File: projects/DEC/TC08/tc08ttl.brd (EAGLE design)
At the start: 393.8 x 298.4 mm, 144 parts, among them IC1 74LS30N, IC2 74LS00N, IC3 74LS04N, IC4 74LS74N, IC5 74LS74N, IC6 74LS30N, IC7 74LS00N, IC8 74LS00N, IC9 74LS04N

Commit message: Removed power polygons for signal "NC" from nearly all drawings.  It is cleaner to just approve the unconnected input pins.  The exception is the W707, which has unconnected power pins.  Those would otherwise be connected implicitly, so an explicit "NC" is needed.
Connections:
- removed net NC: A04.T2, A04.V2, A05.E2, A05.H2, A05.T2, A05.V2, A18.H2, A18.L2, A18.M2, A20.H2, A20.L2, A20.M2, A21.H2, A21.L2, A21.M2, A24.A2, A24.B2, A24.J2, A26.D1, AB01.BN1, AB01.BP1, B05.L2, B18.H2, B18.L2, B18.M2, B20.H2, B20.L2, B20.M2, B22.R2, C02.P2, C02.S2, C03.P2, C03.S2, C03.U2, C07.N1, C07.P1, C07.R1, C07.S2, C07.T2, C07.U2, D04.T2, D04.V2, D05.E2, D05.H2, D05.T2, D05.V2, D14.B1, D14.D1, D14.E1, D14.F1, D14.J1, D14.N2, D14.P2, D14.R2, D14.S2, D14.U2, D15.M2, D15.P2, D15.R2, D15.T2
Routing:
- removed copper zone on layer 8, net NC
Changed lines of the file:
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@@
 <layer number="6" name="Route6" color="1" fill="8" visible="no" active="no"/>
 <layer number="7" name="Route7" color="4" fill="8" visible="no" active="no"/>
-<layer number="8" name="NC$" color="1" fill="2" visible="yes" active="yes"/>
 <layer number="9" name="Route9" color="4" fill="2" visible="no" active="no"/>
 <layer number="10" name="Route10" color="1" fill="7" visible="no" active="no"/>
@@
 <contactref element="C14" pad="A1"/>
 <contactref element="C14" pad="D1"/>
-<contactref element="C14" pad="K1"/>
 <contactref element="C14" pad="F2"/>
-<wire x1="207.9625" y1="142.875" x2="204.7875" y2="133.35" width="0" layer="19" extent="1-1"/>
-<wire x1="204.7875" y1="133.35" x2="198.4375" y2="127" width="0" layer="19" extent="1-1"/>
-<wire x1="198.4375" y1="127" x2="201.6125" y2="117.475" width="0" layer="19" extent="1-1"/>
+<contactref element="C14" pad="K1"/>
+<wire x1="204.7875" y1="133.35" x2="207.9625" y2="142.875" width="0" layer="19" extent="1-1"/>
+<wire x1="198.4375" y1="127" x2="204.7875" y2="133.35" width="0" layer="19" extent="1-1"/>
+<wire x1="201.6125" y1="117.475" x2="198.4375" y2="127" width="0" layer="19" extent="1-1"/>
 <wire x1="207.9625" y1="117.475" x2="201.6125" y2="117.475" width="0" layer="19" extent="1-1"/>
-<wire x1="198.4375" y1="127" x2="176.2125" y2="123.825" width="0" layer="19" extent="1-1"/>
-<wire x1="201.6125" y1="117.475" x2="195.2625" y2="92.075" width="0" layer="19" extent="1-1"/>
+<wire x1="176.2125" y1="123.825" x2="198.4375" y2="127" width="0" layer="19" extent="1-1"/>
+<wire x1="195.2625" y1="92.075" x2="201.6125" y2="117.475" width="0" layer="19" extent="1-1"/>
 </signal>
 <signal name="N$17">
@@
 <contactref element="A21" pad="V2"/>
 </signal>
-<signal name="NC">
-<contactref element="AB01" pad="BN1"/>
-<contactref element="AB01" pad="BP1"/>
-<contactref element="A04" pad="T2"/>
-<contactref element="A04" pad="V2"/>
-<contactref element="A05" pad="T2"/>
-<contactref element="A05" pad="V2"/>
-<contactref element="A24" pad="A2"/>
-<contactref element="A24" pad="B2"/>
-<contactref element="A26" pad="D1"/>
-<contactref element="A05" pad="E2"/>
-<contactref element="A05" pad="H2"/>
-<contactref element="D05" pad="T2"/>
-<contactref element="D05" pad="V2"/>
-<contactref element="D04" pad="V2"/>
-<contactref element="D04" pad="T2"/>
-<contactref element="D05" pad="E2"/>
-<contactref element="D05" pad="H2"/>
-<contactref element="A24" pad="J2"/>
-<contactref element="C07" pad="U2"/>
-<contactref element="C07" pad="S2"/>
-<contactref element="C07" pad="T2"/>
-<contactref element="C07" pad="P1"/>
-<contactref element="C07" pad="N1"/>
-<contactref element="C07" pad="R1"/>
-<contactref element="B22" pad="R2"/>
-<contactref element="D15" pad="M2"/>
-<contactref element="D15" pad="R2"/>
-<contactref element="D15" pad="T2"/>
-<contactref element="D15" pad="P2"/>
-<contactref element="D14" pad="U2"/>
-<contactref element="D14" pad="S2"/>
-<contactref element="D14" pad="R2"/>
-<contactref element="D14" pad="P2"/>
-<contactref element="D14" pad="N2"/>
-<contactref element="A21" pad="M2"/>
-<contactref element="A21" pad="L2"/>
-<contactref element="A21" pad="H2"/>
-<contactref element="B20" pad="H2"/>
-<contactref element="B20" pad="M2"/>
-<contactref element="B20" pad="L2"/>
-<contactref element="A20" pad="L2"/>
-<contactref element="A20" pad="M2"/>
-<contactref element="A20" pad="H2"/>
-<contactref element="B18" pad="H2"/>
-<contactref element="B18" pad="M2"/>
-<contactref element="B18" pad="L2"/>
-<contactref element="A18" pad="L2"/>
-<contactref element="A18" pad="H2"/>
-<contactref element="A18" pad="M2"/>
-<contactref element="B05" pad="L2"/>
-<contactref element="C02" pad="S2"/>
-<contactref element="C02" pad="P2"/>
-<contactref element="C03" pad="P2"/>
-<contactref element="C03" pad="S2"/>
-<contactref element="C03" pad="U2"/>
-<contactref element="D14" pad="D1"/>
-<contactref element="D14" pad="B1"/>
-<contactref element="D14" pad="E1"/>
-<contactref element="D14" pad="F1"/>
-<contactref element="D14" pad="J1"/>
-<polygon width="0.254" layer="8" orphans="yes">
-<vertex x="-0.0358" y="0.0126"/>
-<vertex x="414.02" y="0.0126"/>
-<vertex x="414.02" y="298.4501"/>
-<vertex x="-0.0358" y="298.4501"/>
-</polygon>
-</signal>
 <signal name="+11V">

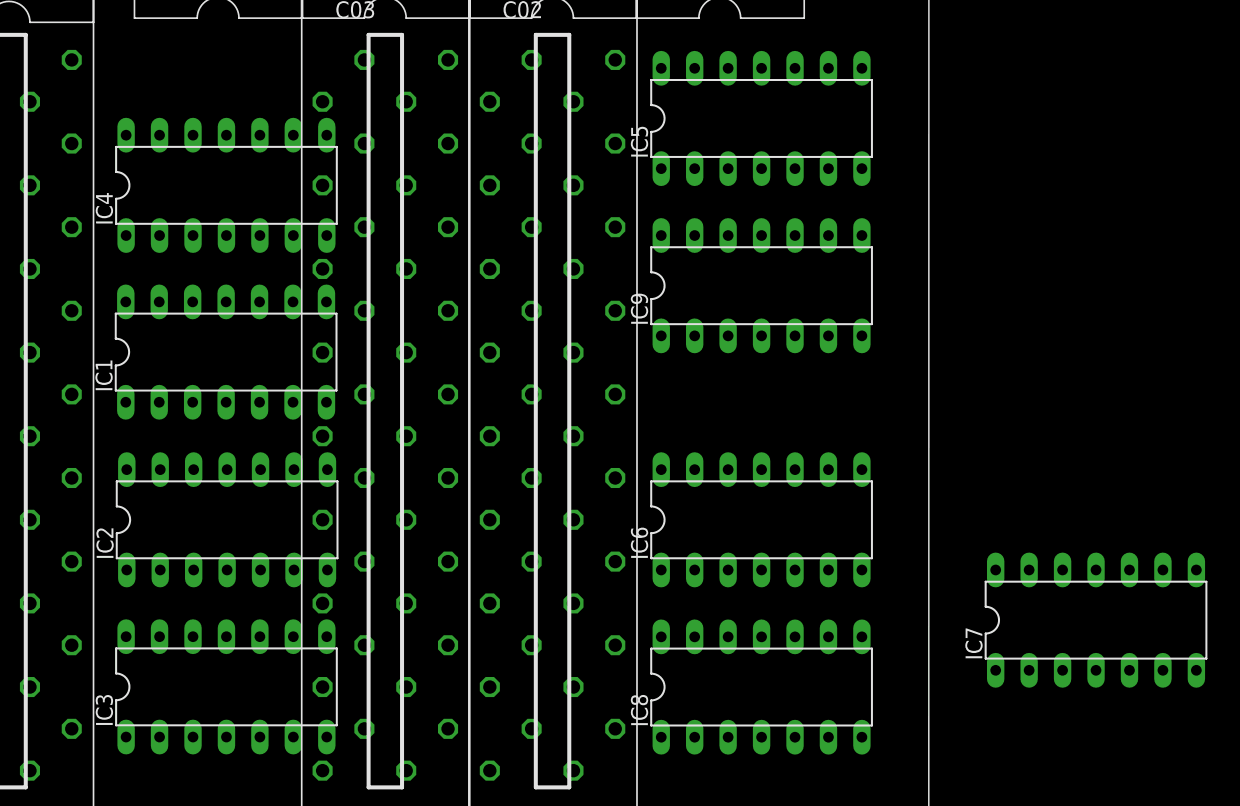
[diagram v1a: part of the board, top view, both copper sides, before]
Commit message: Where possible, map 74xx-jameco to 74xx-us. Moved the 7438 to dec-con.lbr. Also changed the spelling of CRYTAL to CRYSTAL.
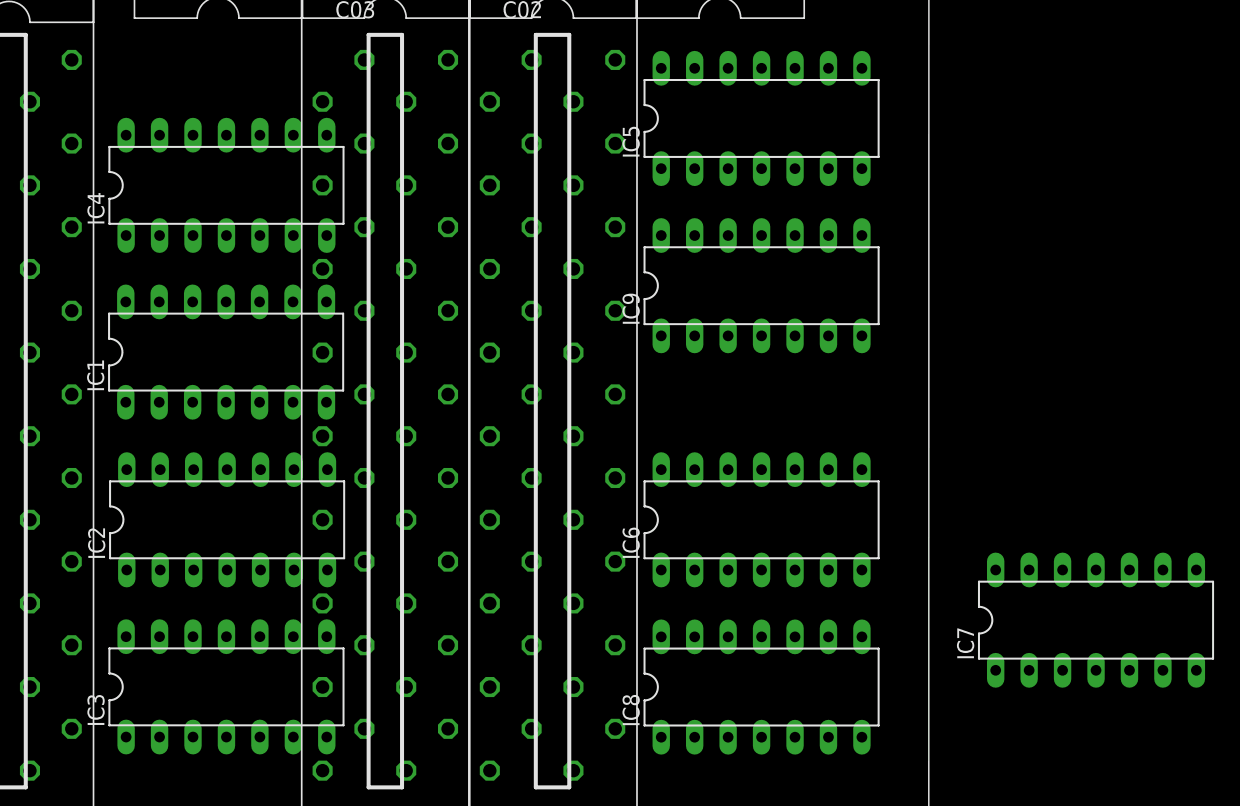
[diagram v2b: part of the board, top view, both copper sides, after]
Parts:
- IC1, IC2, IC3, IC4, IC5, IC6, IC7, IC8, IC9: device 74xx-jameco:DIL14 -> 74xx-us:DIL14
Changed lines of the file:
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@@
 <layer number="6" name="Route6" color="1" fill="8" visible="no" active="no"/>
 <layer number="7" name="Route7" color="4" fill="8" visible="no" active="no"/>
+<layer number="8" name="Route8" color="1" fill="2" visible="no" active="no"/>
 <layer number="9" name="Route9" color="4" fill="2" visible="no" active="no"/>
 <layer number="10" name="Route10" color="1" fill="7" visible="no" active="no"/>
@@
 <element name="U$87" library="holes" package="4,3" value="" x="53.975" y="80.9625"/>
 <element name="U$88" library="holes" package="4,3" value="" x="15.875" y="80.9625"/>
-<element name="IC1" library="74xx-jameco" package="DIL14" value="74LS30N" x="340.3346" y="120.6881"/>
-<element name="IC2" library="74xx-jameco" package="DIL14" value="74LS00N" x="340.4108" y="107.95"/>
-<element name="IC3" library="74xx-jameco" package="DIL14" value="74LS04N" x="340.36" y="95.2627"/>
-<element name="IC4" library="74xx-jameco" package="DIL14" value="74LS74N" x="340.36" y="133.35"/>
-<element name="IC5" library="74xx-jameco" package="DIL14" value="74LS74N" x="381" y="138.43"/>
-<element name="IC6" library="74xx-jameco" package="DIL14" value="74LS30N" x="381" y="107.95"/>
-<element name="IC7" library="74xx-jameco" package="DIL14" value="74LS00N" x="406.4" y="100.33"/>
-<element name="IC8" library="74xx-jameco" package="DIL14" value="74LS00N" x="381" y="95.25"/>
-<element name="IC9" library="74xx-jameco" package="DIL14" value="74LS04N" x="381" y="125.73"/>
+<element name="IC1" library="74xx-us" package="DIL14" value="74LS30N" x="340.3346" y="120.6881"/>
+<element name="IC2" library="74xx-us" package="DIL14" value="74LS00N" x="340.4108" y="107.95"/>
+<element name="IC3" library="74xx-us" package="DIL14" value="74LS04N" x="340.36" y="95.2627"/>
+<element name="IC4" library="74xx-us" package="DIL14" value="74LS74N" x="340.36" y="133.35"/>
+<element name="IC5" library="74xx-us" package="DIL14" value="74LS74N" x="381" y="138.43"/>
+<element name="IC6" library="74xx-us" package="DIL14" value="74LS30N" x="381" y="107.95"/>
+<element name="IC7" library="74xx-us" package="DIL14" value="74LS00N" x="406.4" y="100.33"/>
+<element name="IC8" library="74xx-us" package="DIL14" value="74LS00N" x="381" y="95.25"/>
+<element name="IC9" library="74xx-us" package="DIL14" value="74LS04N" x="381" y="125.73"/>
 </elements>
 <signals>
